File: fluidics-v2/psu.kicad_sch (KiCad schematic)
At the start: 13 parts, among them U2 D24V10FX, U3 U3V50F24, U4 AP7366EA-33W5-7

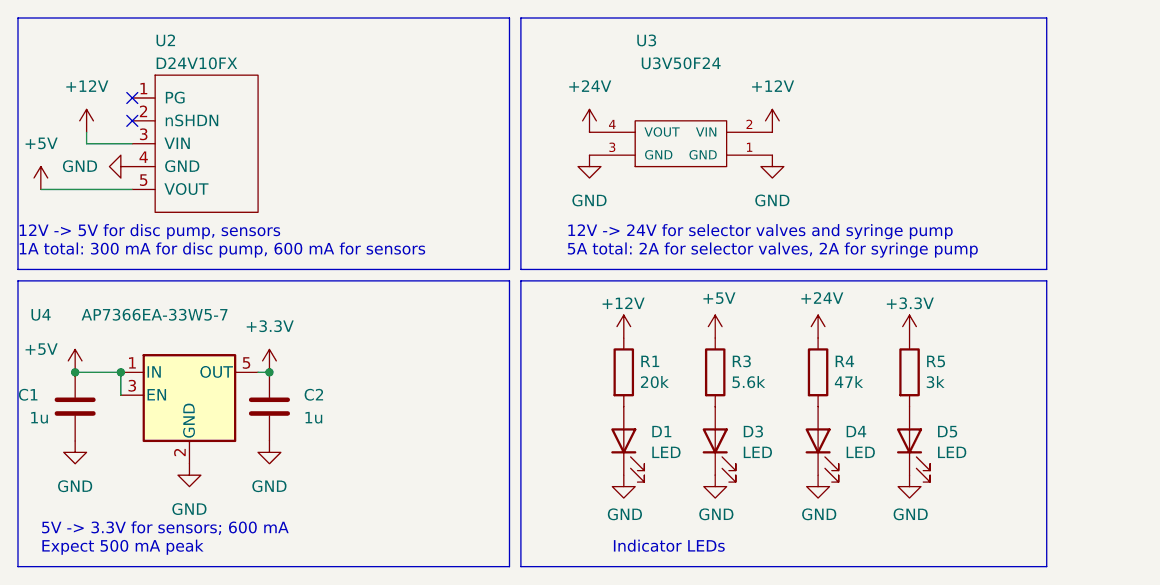
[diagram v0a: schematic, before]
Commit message: added footprints and mounting holes, cleaned up some sheets
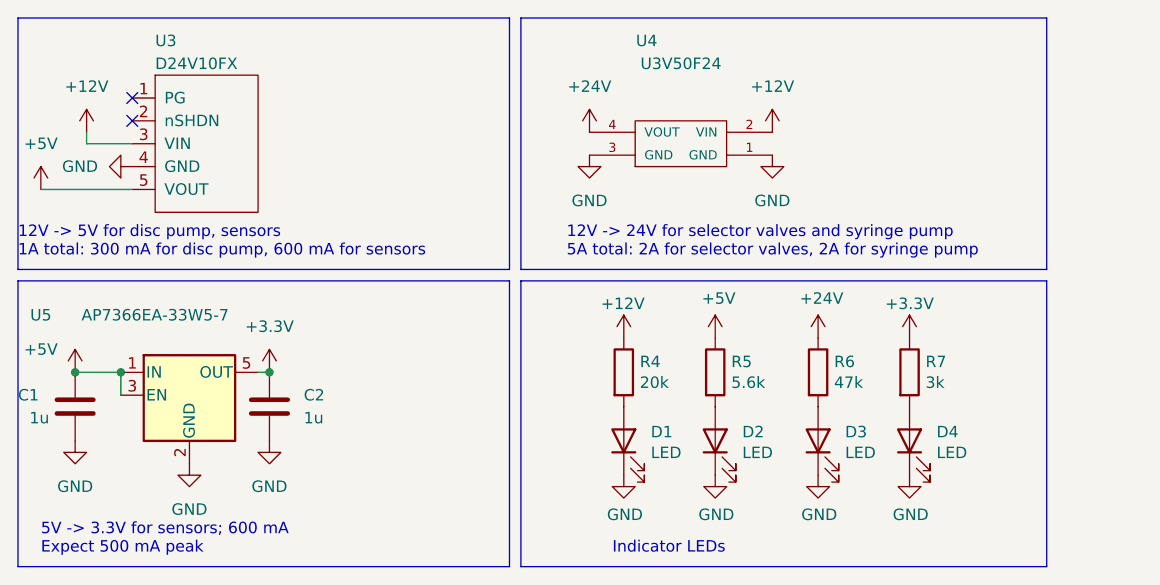
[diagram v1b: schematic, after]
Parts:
- renumbered D3 to D2, D4 to D3, D5 to D4, R1 to R4, R3 to R5, R4 to R6, R5 to R7, U2 to U3, U3 to U4, U4 to U5

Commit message: started layout
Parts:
- renumbered C1 to C2, C2 to C3, U5 to U4, U3 to U5, U4 to U6

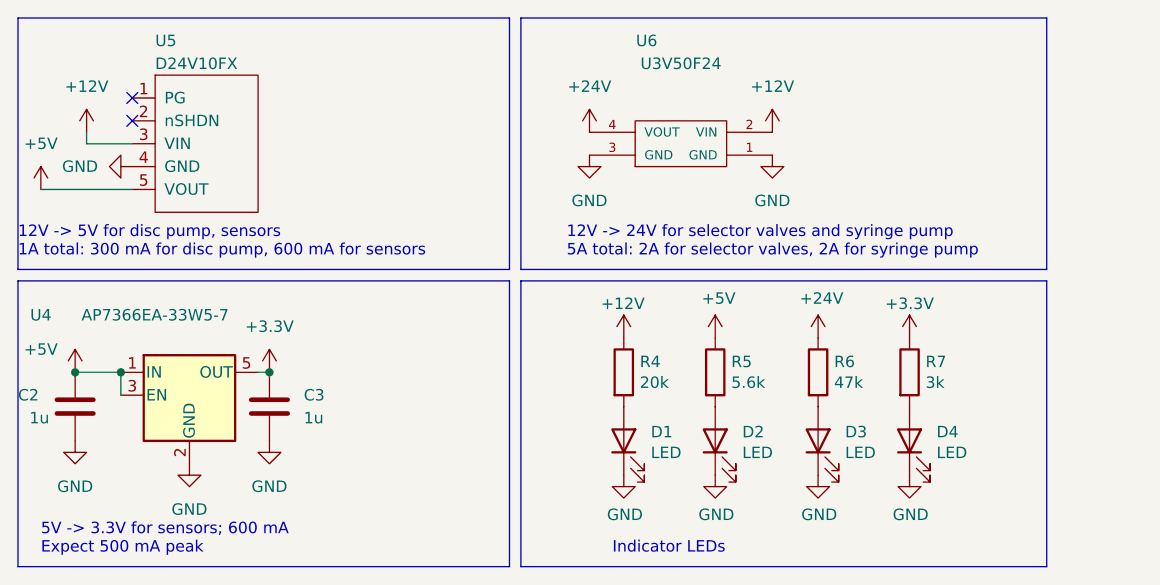
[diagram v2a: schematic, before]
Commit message: added new connector for motor control daughter board. began layout
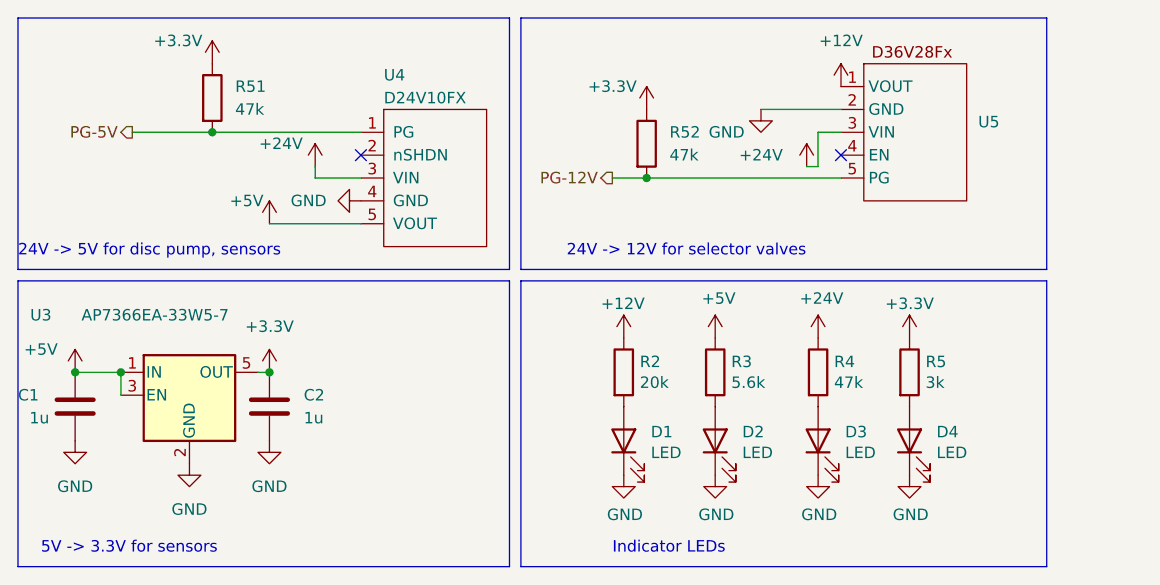
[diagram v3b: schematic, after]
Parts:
- removed U6: U3V50F24, pololu:U3V50F24, symbol pololu:U3V50F24
- added R51, R52: 47k, Resistor_SMD:R_0603_1608Metric_Pad0.98x0.95mm_HandSolder, symbol Device:R
- added U5: ~, D36V28Fx:D36V28Fx, symbol D36V28Fx:D36V28FX
- renumbered C2 to C1, C3 to C2, R4 to R2, R5 to R3, R6 to R4, R7 to R5, U4 to U3, U5 to U4
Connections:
- net +12V: now also U5.1 (VOUT); no longer U4.3 (VIN)
- net +24V: now also U4.3 (VIN), U5.3 (VIN)
- net +3.3V: now also R51.1, R52.1
- net GND: now also U5.2 (GND)
- net PG-5V: now reaches U4.1 (PG)
- net PG-5V: now also R51.2
- new net PG-12V: R52.2, U5.5 (PG)
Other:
- note added: "24V -> 12V for selector valves"
- note added: "24V -> 5V for disc pump, sensors"
- note added: "5V -> 3.3V for sensors"
- note removed: "12V -> 24V for selector valves and syringe pump 5A total: 2A for selector valves, 2A for syringe pump"
- note removed: "12V -> 5V for disc pump, sensors 1A total: 300 mA for disc pump, 600 mA for sensors"
- note removed: "5V -> 3.3V for sensors; 600 mA Expect 500 mA peak"
- moved on the sheet: U4
